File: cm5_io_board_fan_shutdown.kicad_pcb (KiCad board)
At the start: 2 copper layers, 15.5 x 49.5 mm, 33 parts, among them J1 Conn_Pi_JST_SH, J2 Conn_Fan_JST_SH, J3 Conn_Fan_Header, Q1 AO3401A, Q2 BSS138, Q3 BSS138, U1 LM393

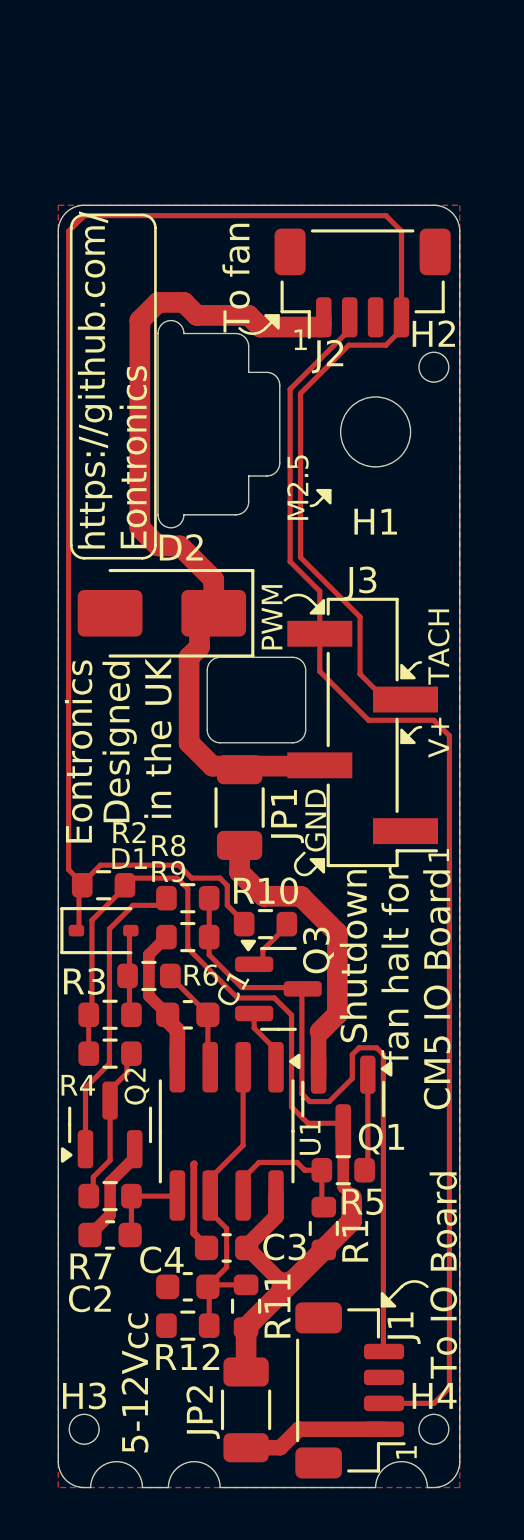
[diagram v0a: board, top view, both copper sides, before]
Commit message: [fix_output_drive] Updated PCB layout to reflect output FET flip in schematic and resistor divider on gate
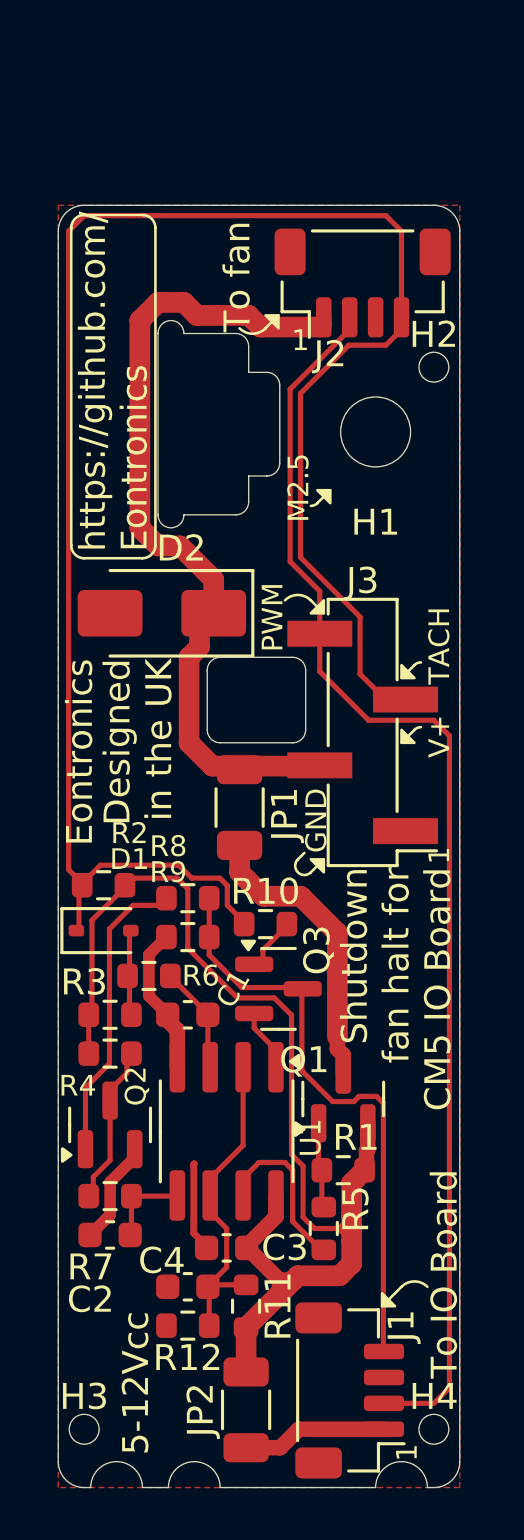
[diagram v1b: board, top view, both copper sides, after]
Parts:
- R5: value 6.8k -> 20k
- moved R1 2.37 mm to (173.8, 78.5), turned to 0 degrees
- moved R5 2.37 mm to (173.0, 80.8), turned to 90 degrees
- turned Q1 to 90 degrees
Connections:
- Q1 pad 2: Net-(JP1-A) -> VCC
- Q1 pad 3: VCC -> Net-(JP1-A)
- R1 pad 1: Net-(R1-Pad1) -> Net-(Q1-G)
- R5 pad 1: Net-(R1-Pad1) -> Net-(R5-Pad1)
- U1 pad 7: Net-(R1-Pad1) -> Net-(R5-Pad1)
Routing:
- net VCC: track 39.7 -> 46.5 mm
- net Net-(R5-Pad1): track 0.00 -> 6.58 mm
- net Net-(R1-Pad1): track 5.54 -> 0.00 mm
- net TACH_PI: track 26.6 -> 22.9 mm
